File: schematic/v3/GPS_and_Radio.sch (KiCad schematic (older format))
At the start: 16 parts

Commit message: Small cleanup
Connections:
- wire segments 106 -> 107
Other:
- note added: "GPS Module"
- note added: "RN Module"
- moved on the sheet: C?, J?, R?, U?

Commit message: Started PCB layout
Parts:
- C12, C13, C23, C24, C25, C3, C5: renamed from C?; footprint (none) -> Capacitors_SMD:C_0805
- R10, R2, R3: renamed from R?; footprint (none) -> Resistors_SMD:R_0805
- gave numbers to parts that had none: 6
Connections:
- net labels removed: V_bak

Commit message: Started layout work
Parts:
- C12, C13, C23, C24, C25, C3, C5: symbol Device:C -> gps_node-rescue:C-Device
- R10, R2, R3: symbol Device:R -> gps_node-rescue:R-Device
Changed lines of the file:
@@
 $EndComp
 $Comp
-L power:GND #PWR?
+L gps_node-rescue:GND-power #PWR?
 U 1 1 5C37B0BE
 P 2800 3100
@@
 $EndComp
 $Comp
-L power:GND #PWR?
+L gps_node-rescue:GND-power #PWR?
 U 1 1 5C37B0C4
 P 2950 3100
@@
 $EndComp
 $Comp
-L power:GND #PWR?
+L gps_node-rescue:GND-power #PWR?
 U 1 1 5C37B0CA
 P 3250 3100
@@
 $EndComp
 $Comp
-L power:GND #PWR?
+L gps_node-rescue:GND-power #PWR?
 U 1 1 5C37B0D0
 P 2350 3500
@@
 $EndComp
 $Comp
-L power:GND #PWR?
+L gps_node-rescue:GND-power #PWR?
 U 1 1 5C37B0D6
 P 4150 3500
@@
 $EndComp
 $Comp
-L power:GND #PWR?
+L gps_node-rescue:GND-power #PWR?
 U 1 1 5C37B0EE
 P 4250 5500
@@
 $EndComp
 $Comp
-L power:GND #PWR?
+L gps_node-rescue:GND-power #PWR?
 U 1 1 5C37B0F4
 P 4150 4700
@@
 $EndComp
 $Comp
-L power:GND #PWR?
+L gps_node-rescue:GND-power #PWR?
 U 1 1 5C37B0FA
 P 4150 4400
@@
 NoConn ~ 2350 5300
 $Comp
-L power:GND #PWR?
+L gps_node-rescue:GND-power #PWR?
 U 1 1 5C37B114
 P 2400 6500
@@
 $EndComp
 $Comp
-L power:GND #PWR?
+L gps_node-rescue:GND-power #PWR?
 U 1 1 5C37B13C
 P 7850 3050
@@
 $EndComp
 $Comp
-L power:GND #PWR?
+L gps_node-rescue:GND-power #PWR?
 U 1 1 5C37B142
 P 7450 3050
@@
 NoConn ~ 7750 3050
 $Comp
-L power:GND #PWR?
+L gps_node-rescue:GND-power #PWR?
 U 1 1 5C37B175
 P 8600 5000
@@
 $EndComp
 $Comp
-L power:GND #PWR?
+L gps_node-rescue:GND-power #PWR?
 U 1 1 5C37B188
 P 3550 3100
@@
 $EndComp
 $Comp
-L power:GND #PWR?
+L gps_node-rescue:GND-power #PWR?
 U 1 1 5C37B18E
 P 3700 3100
@@
 $EndComp
 $Comp
-L power:+3V3 #PWR?
+L gps_node-rescue:+3V3-power #PWR?
 U 1 1 5C37B1E2
 P 1150 1500
@@
 $EndComp
 $Comp
-L power:GND #PWR?
+L gps_node-rescue:GND-power #PWR?
 U 1 1 5C37B1E9
 P 1650 2100
@@
 	3400 2600 3850 2600
 $Comp
-L power:GND #PWR?
+L gps_node-rescue:GND-power #PWR?
 U 1 1 5C37B1FC
 P 4000 2800
@@
 $EndComp
 $Comp
-L power:+3V3 #PWR?
+L gps_node-rescue:+3V3-power #PWR?
 U 1 1 5C3814CC
 P 5850 6800
@@
 GND
 $Comp
-L power:GND #PWR?
+L gps_node-rescue:GND-power #PWR?
 U 1 1 5C3814D7
 P 5550 7300
@@
 V_BAK
 $Comp
-L power:VBUS #PWR?
+L gps_node-rescue:VBUS-power #PWR?
 U 1 1 5C3814E0
 P 5700 6650
@@
 $EndComp
 $Comp
-L power:+BATT #PWR?
+L gps_node-rescue:+BATT-power #PWR?
 U 1 1 5C3814E6
 P 5550 6500
@@
 Global power labels
 $Comp
-L Device:C C5
+L gps_node-rescue:C-Device C5
 U 1 1 5C386246
 P 2000 1850
@@
 	1650 1850 1650 2050
 $Comp
-L Device:C C12
+L gps_node-rescue:C-Device C12
 U 1 1 5C393EFC
 P 2450 1850
@@
 $EndComp
 $Comp
-L Device:C C23
+L gps_node-rescue:C-Device C23
 U 1 1 5C393F92
 P 2800 1850
@@
 $EndComp
 $Comp
-L Device:C C24
+L gps_node-rescue:C-Device C24
 U 1 1 5C393FCC
 P 3150 1850
@@
 $EndComp
 $Comp
-L power:+3V3 #PWR?
+L gps_node-rescue:+3V3-power #PWR?
 U 1 1 5C3A7287
 P 6450 1550
@@
 $EndComp
 $Comp
-L power:GND #PWR?
+L gps_node-rescue:GND-power #PWR?
 U 1 1 5C3A728D
 P 6950 2150
@@
 $EndComp
 $Comp
-L Device:C C3
+L gps_node-rescue:C-Device C3
 U 1 1 5C3A7293
 P 7300 1900
@@
 	6950 1900 6950 2100
 $Comp
-L Device:C C13
+L gps_node-rescue:C-Device C13
 U 1 1 5C3A729D
 P 7750 1900
@@
 $EndComp
 $Comp
-L Device:C C25
+L gps_node-rescue:C-Device C25
 U 1 1 5C3A72A4
 P 8100 1900
@@
 	6450 4450 6900 4450
 $Comp
-L power:GND #PWR?
+L gps_node-rescue:GND-power #PWR?
 U 1 1 5C3D3B3F
 P 6700 4150
@@
 	6700 4050 6900 4050
 $Comp
-L power:GND #PWR?
+L gps_node-rescue:GND-power #PWR?
 U 1 1 5C40A6F7
 P 6700 5000
@@
 	6700 4950 6700 5000
 $Comp
-L Device:R R3
+L gps_node-rescue:R-Device R3
 U 1 1 5C41C2A5
 P 8650 3850
@@
 $EndComp
 $Comp
-L Device:R R2
+L gps_node-rescue:R-Device R2
 U 1 1 5C41C3FB
 P 8650 3750
@@
 	4250 5400 4150 5400
 $Comp
-L power:GND #PWR?
+L gps_node-rescue:GND-power #PWR?
 U 1 1 5C435A06
 P 2250 5500
@@
 	1500 3350 1200 3350
 $Comp
-L Device:R R10
+L gps_node-rescue:R-Device R10
 U 1 1 5C4434B7
 P 1500 3650

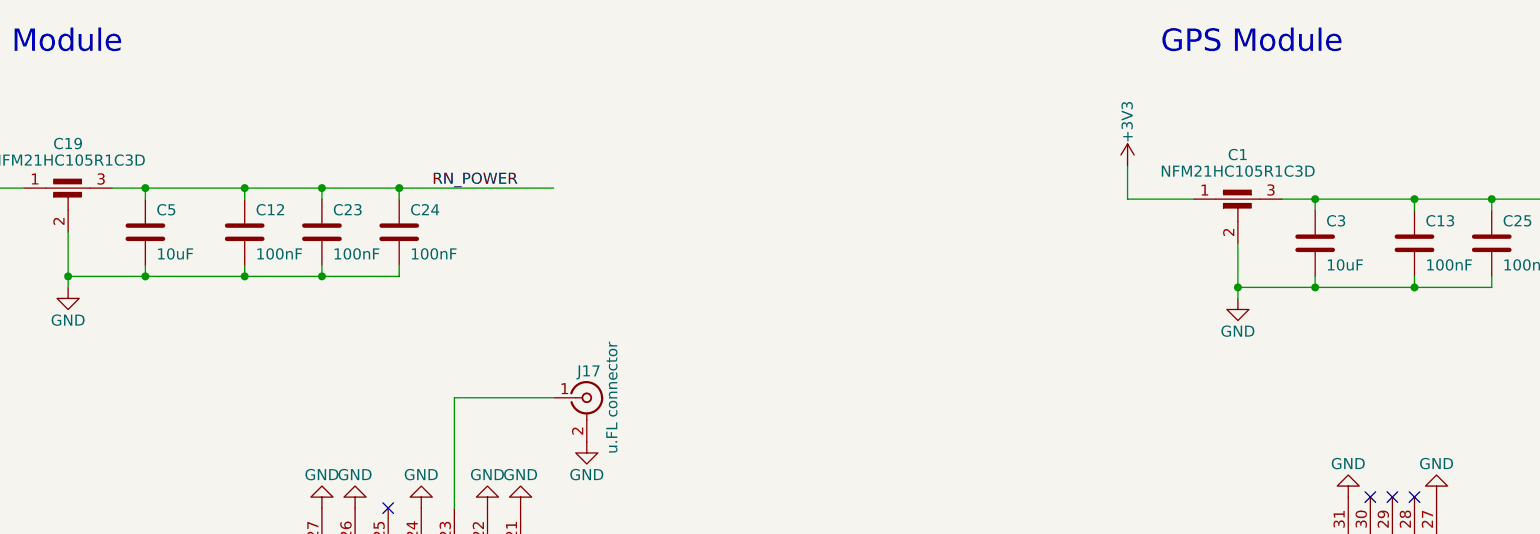
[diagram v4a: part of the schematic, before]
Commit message: Replace 10uF by 4.7uF and clean up power circuit
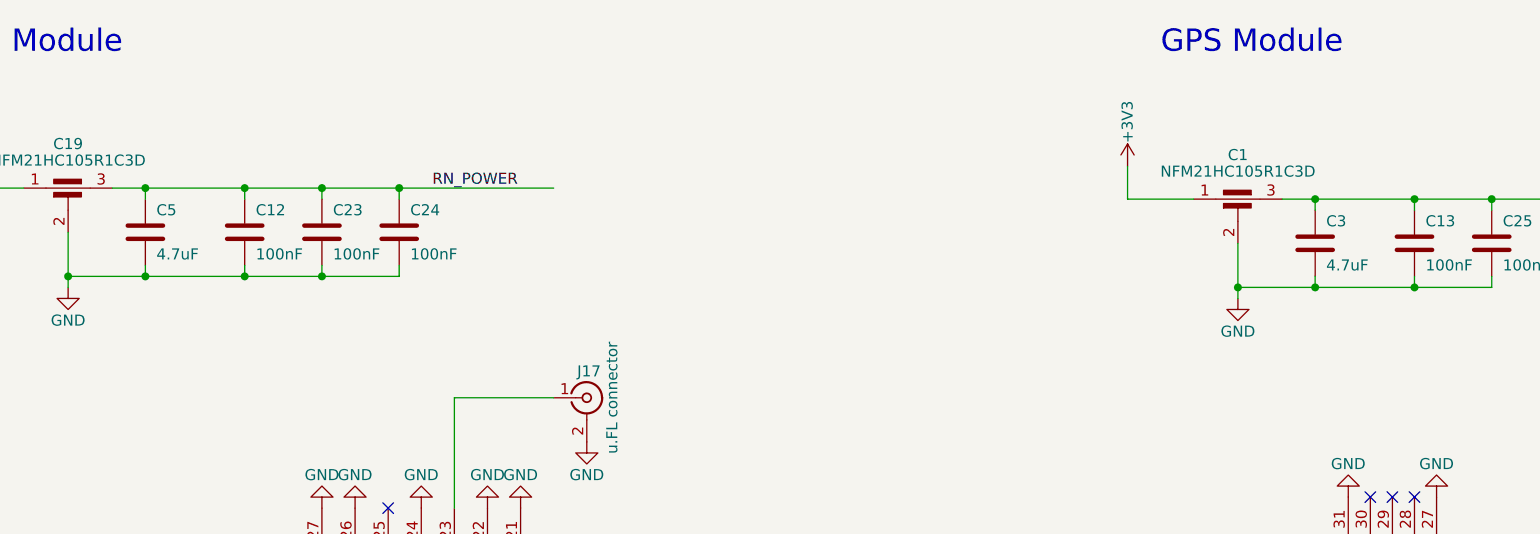
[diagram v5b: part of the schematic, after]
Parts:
- C3, C5: value 10uF -> 4.7uF
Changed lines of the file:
@@
 P 2000 1850
 F 0 "C5" H 2050 1950 50  0000 L CNN
-F 1 "10uF" H 2050 1750 50  0000 L CNN
+F 1 "4.7uF" H 2050 1750 50  0000 L CNN
 F 2 "Capacitors_SMD:C_0805" H 2038 1700 50  0001 C CNN
 F 3 "~" H 2000 1850 50  0001 C CNN
@@
 P 7300 1900
 F 0 "C3" H 7350 2000 50  0000 L CNN
-F 1 "10uF" H 7350 1800 50  0000 L CNN
+F 1 "4.7uF" H 7350 1800 50  0000 L CNN
 F 2 "Capacitors_SMD:C_0805" H 7338 1750 50  0001 C CNN
 F 3 "~" H 7300 1900 50  0001 C CNN

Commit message: Cleaned up schematic
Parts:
- C12, C13, C23, C24, C25, C3, C5: footprint Capacitors_SMD:C_0805 -> Capacitor_SMD:C_0805_2012Metric
- J16: footprint Pin_Headers:Pin_Header_Straight_1x06_Pitch2.54mm -> Connector_PinHeader_2.54mm:PinHeader_1x06_P2.54mm_Vertical
- R10, R2, R3: footprint Resistors_SMD:R_0805 -> Resistor_SMD:R_0805_2012Metric
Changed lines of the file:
@@
 F 0 "C5" H 2050 1950 50  0000 L CNN
 F 1 "4.7uF" H 2050 1750 50  0000 L CNN
-F 2 "Capacitors_SMD:C_0805" H 2038 1700 50  0001 C CNN
+F 2 "Capacitor_SMD:C_0805_2012Metric" H 2038 1700 50  0001 C CNN
 F 3 "~" H 2000 1850 50  0001 C CNN
 	1    2000 1850
@@
 F 0 "C12" H 2500 1950 50  0000 L CNN
 F 1 "100nF" H 2500 1750 50  0000 L CNN
-F 2 "Capacitors_SMD:C_0805" H 2488 1700 50  0001 C CNN
+F 2 "Capacitor_SMD:C_0805_2012Metric" H 2488 1700 50  0001 C CNN
 F 3 "~" H 2450 1850 50  0001 C CNN
 	1    2450 1850
@@
 F 0 "C23" H 2850 1950 50  0000 L CNN
 F 1 "100nF" H 2850 1750 50  0000 L CNN
-F 2 "Capacitors_SMD:C_0805" H 2838 1700 50  0001 C CNN
+F 2 "Capacitor_SMD:C_0805_2012Metric" H 2838 1700 50  0001 C CNN
 F 3 "~" H 2800 1850 50  0001 C CNN
 	1    2800 1850
@@
 F 0 "C24" H 3200 1950 50  0000 L CNN
 F 1 "100nF" H 3200 1750 50  0000 L CNN
-F 2 "Capacitors_SMD:C_0805" H 3188 1700 50  0001 C CNN
+F 2 "Capacitor_SMD:C_0805_2012Metric" H 3188 1700 50  0001 C CNN
 F 3 "~" H 3150 1850 50  0001 C CNN
 	1    3150 1850
@@
 F 0 "C3" H 7350 2000 50  0000 L CNN
 F 1 "4.7uF" H 7350 1800 50  0000 L CNN
-F 2 "Capacitors_SMD:C_0805" H 7338 1750 50  0001 C CNN
+F 2 "Capacitor_SMD:C_0805_2012Metric" H 7338 1750 50  0001 C CNN
 F 3 "~" H 7300 1900 50  0001 C CNN
 	1    7300 1900
@@
 F 0 "C13" H 7800 2000 50  0000 L CNN
 F 1 "100nF" H 7800 1800 50  0000 L CNN
-F 2 "Capacitors_SMD:C_0805" H 7788 1750 50  0001 C CNN
+F 2 "Capacitor_SMD:C_0805_2012Metric" H 7788 1750 50  0001 C CNN
 F 3 "~" H 7750 1900 50  0001 C CNN
 	1    7750 1900
@@
 F 0 "C25" H 8150 2000 50  0000 L CNN
 F 1 "100nF" H 8150 1800 50  0000 L CNN
-F 2 "Capacitors_SMD:C_0805" H 8138 1750 50  0001 C CNN
+F 2 "Capacitor_SMD:C_0805_2012Metric" H 8138 1750 50  0001 C CNN
 F 3 "~" H 8100 1900 50  0001 C CNN
 	1    8100 1900
@@
 F 0 "R3" V 8750 4000 50  0000 C CNN
 F 1 "220" V 8750 3750 50  0000 C CNN
-F 2 "Resistors_SMD:R_0805" V 8580 3850 50  0001 C CNN
+F 2 "Resistor_SMD:R_0805_2012Metric" V 8580 3850 50  0001 C CNN
 F 3 "~" H 8650 3850 50  0001 C CNN
 	1    8650 3850
@@
 F 0 "R2" V 8750 3900 50  0000 C CNN
 F 1 "220" V 8750 3650 50  0000 C CNN
-F 2 "Resistors_SMD:R_0805" V 8580 3750 50  0001 C CNN
+F 2 "Resistor_SMD:R_0805_2012Metric" V 8580 3750 50  0001 C CNN
 F 3 "~" H 8650 3750 50  0001 C CNN
 	1    8650 3750
@@
 F 0 "R10" H 1570 3696 50  0000 L CNN
 F 1 "10k" H 1570 3605 50  0000 L CNN
-F 2 "Resistors_SMD:R_0805" V 1430 3650 50  0001 C CNN
+F 2 "Resistor_SMD:R_0805_2012Metric" V 1430 3650 50  0001 C CNN
 F 3 "~" H 1500 3650 50  0001 C CNN
 	1    1500 3650
@@
 F 0 "J16" H 1450 6700 50  0000 C CNN
 F 1 "FW_UPDATE" H 1450 6000 50  0000 C CNN
-F 2 "Pin_Headers:Pin_Header_Straight_1x06_Pitch2.54mm" H 1450 6400 50  0001 C CNN
+F 2 "Connector_PinHeader_2.54mm:PinHeader_1x06_P2.54mm_Vertical" H 1450 6400 50  0001 C CNN
 F 3 "" H 1450 6400 50  0001 C CNN
 	1    1450 6400
